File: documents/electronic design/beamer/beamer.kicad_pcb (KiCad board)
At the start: 2 copper layers, 25 parts, among them P1 CONN_01X20, P2 CONN_01X20, T1 2N7002K, T10 2N7002K, T2 2N7002K, T3 2N7002K, T4 2N7002K, T5 2N7002K, T6 2N7002K, T7 2N7002K, T8 2N7002K, T9 2N7002K, U1 NRF24L01-BRKOUT, U2 74HC595D

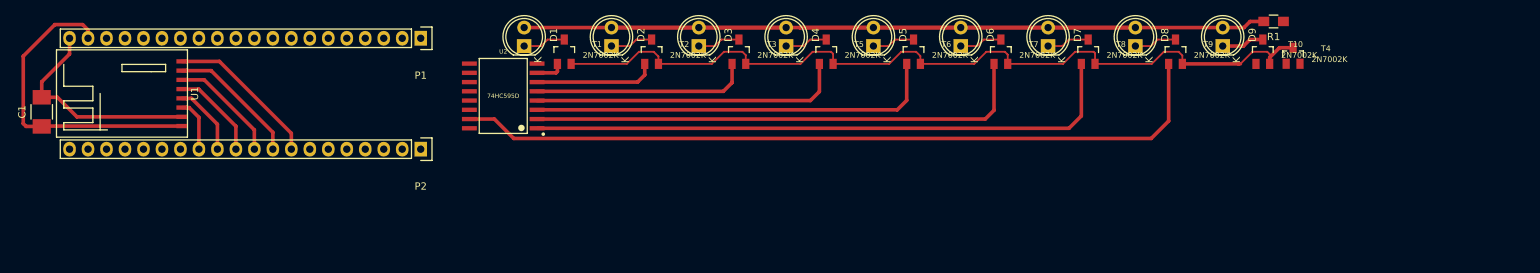
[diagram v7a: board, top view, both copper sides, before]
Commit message: update pcb for beamer with shift registar
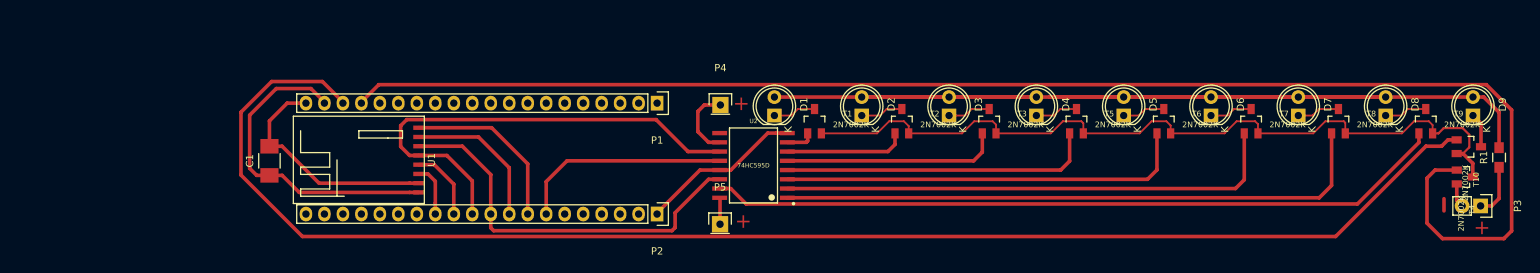
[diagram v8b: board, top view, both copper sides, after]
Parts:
- added P3: CONN_01X02, Pin_Headers:Pin_Header_Straight_1x02, F.Cu at (206.1, 67.4)
- added P4: CONN_01X01, Pin_Headers:Pin_Header_Straight_1x01, F.Cu at (101.6, 53.5)
- added P5: CONN_01X01, Pin_Headers:Pin_Header_Straight_1x01, F.Cu at (101.6, 69.9)
- moved R1 36.2 mm to (208.6, 60.8), turned to 90 degrees
- moved D3 35.7 mm to (133.0, 55.0)
- moved D4 35.7 mm to (145.0, 55.0)
- moved D5 35.7 mm to (157.0, 55.0)
- moved D6 35.7 mm to (169.0, 55.0)
- moved D7 35.7 mm to (181.0, 55.0)
- moved D8 35.7 mm to (193.0, 55.0)
- moved D9 35.7 mm to (205.0, 55.0)
- moved T1 35.7 mm to (114.6, 55.7)
- moved T2 35.7 mm to (126.6, 55.7)
- moved T3 35.7 mm to (138.6, 55.7)
- moved T5 35.7 mm to (150.6, 55.7)
- moved T6 35.7 mm to (162.6, 55.7)
- moved T7 35.7 mm to (174.6, 55.7)
- moved T8 35.7 mm to (186.6, 55.7)
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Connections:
- P1 pad 16: IR_PIN_ID -> Net-(P1-Pad16)
- P1 pad 18: Net-(P1-Pad18) -> IR_PIN_ID
- P2 pad 14: ShiftReg_Expose -> Net-(P2-Pad14)
- P2 pad 7: Net-(P2-Pad7) -> ShiftReg_Expose
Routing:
- net IR_PIN_ID: track 0.00 -> 201.8 mm
- net PWM_38K: track 0.00 -> 201.0 mm
- net SPI1_SCK: track 12.7 -> 65.2 mm
- net SPI1_MOSI: track 15.4 -> 54.6 mm
- net ShiftReg_Expose: track 0.00 -> 29.5 mm
- net GND: track 44.6 -> 71.7 mm
- net +3V3: track 30.1 -> 52.9 mm
- net Net-(T1-Pad2): track 117.5 -> 112.0 mm
- net IR_PIN_8: track 106.0 -> 101.7 mm
- net Net-(D9-Pad1): track 8.92 -> 4.75 mm
- net Net-(D1-Pad2): track 172.5 -> 175.8 mm
- net NRF_IRQ1: track 21.3 -> 23.9 mm
- net SPI1_MISO: track 18.3 -> 20.5 mm
- net (no net): track 0.00 -> 1.68 mm
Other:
- board text added: "+"
